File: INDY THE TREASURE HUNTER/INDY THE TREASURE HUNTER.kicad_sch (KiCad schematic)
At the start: 4 parts, among them J1 Conn_01x06, J2 Conn_01x06, J3 Conn_01x06, J4 Conn_01x06

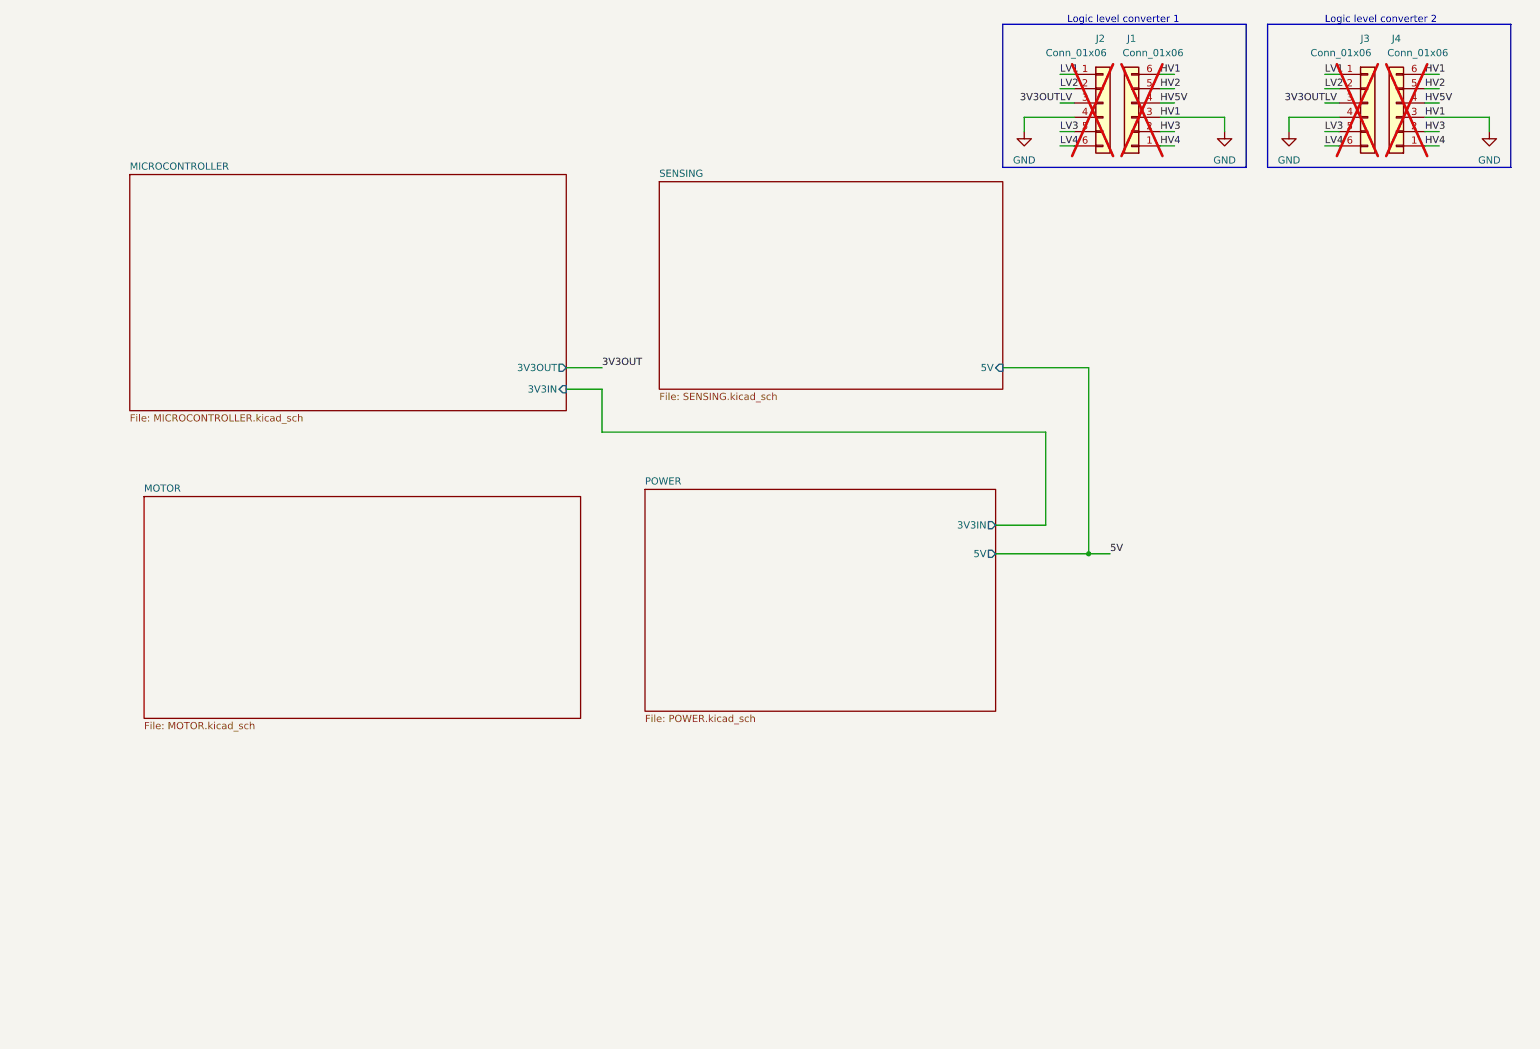
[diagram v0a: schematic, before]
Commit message: 19:16
Got rid of the boxes around the logic level converters, we can neaten those up later it was just becoming a nightmare.

Also IMPORTANT:
Try to stick with this naming convention for logic level lines: NAMEOFLINE_VOLTAGE (eg: ULTRA_TRIG_3V3) so we can track the logic level voltages
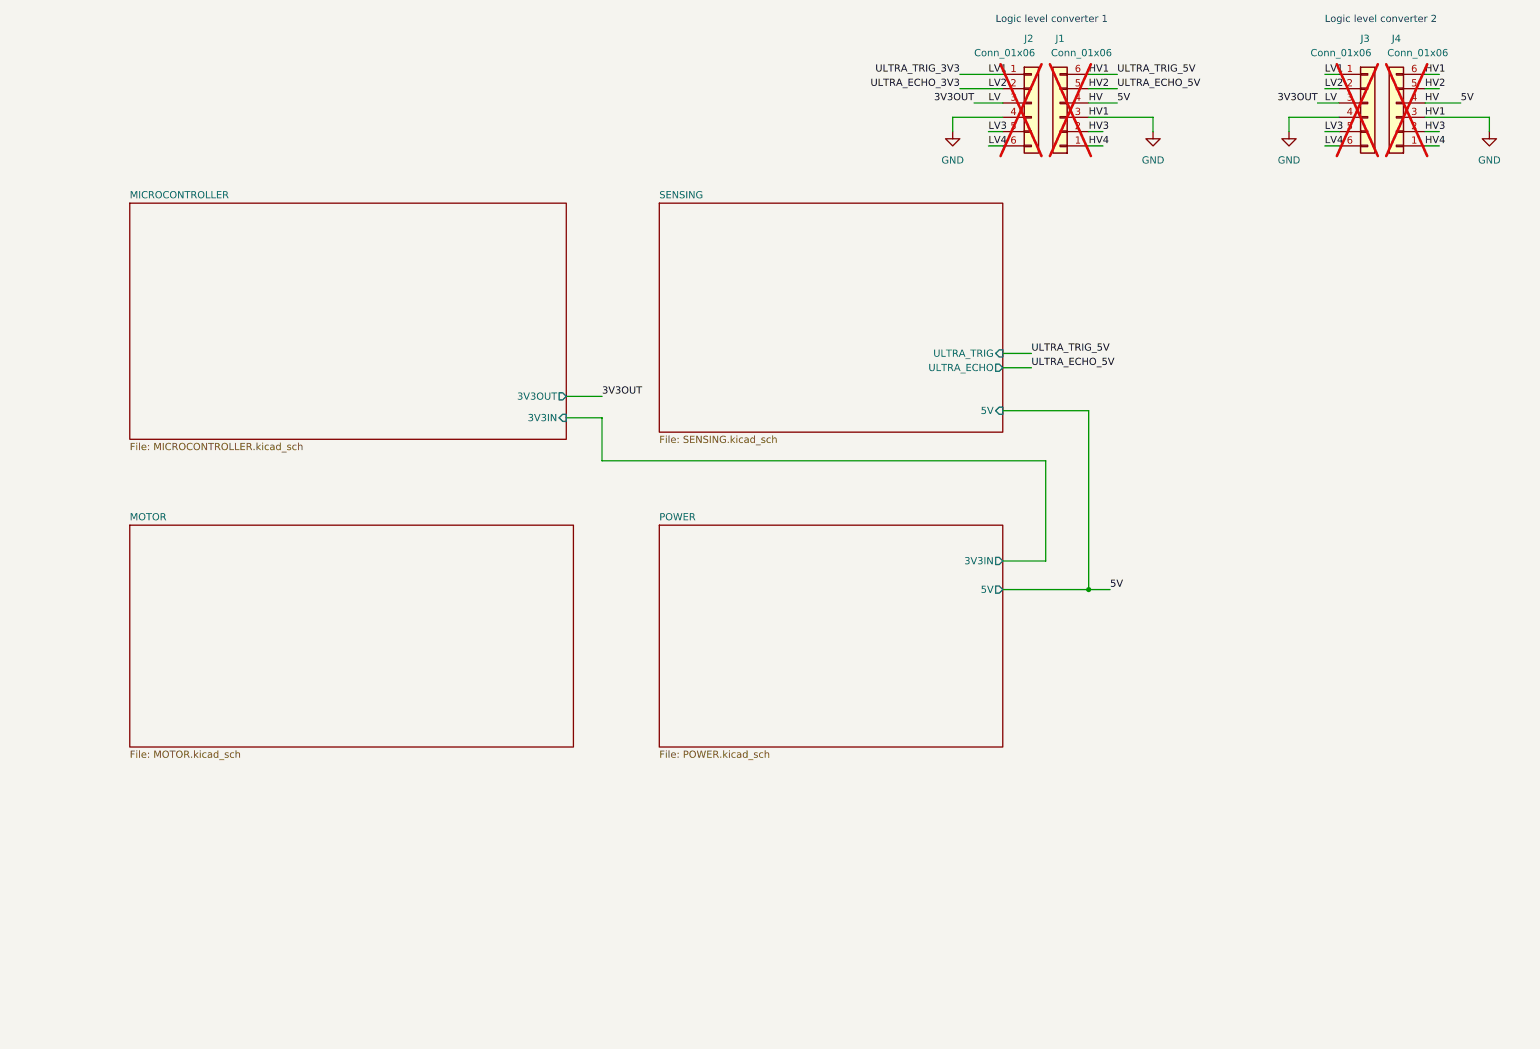
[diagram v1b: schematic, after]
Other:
- sheet SENSING ports: added ULTRA_ECHO, ULTRA_TRIG; removed none
- moved on the sheet: J1, J2

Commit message: Wired up Ultrasonic sensor
I think the USonic sensor is wired up completely. Not that bad actually.
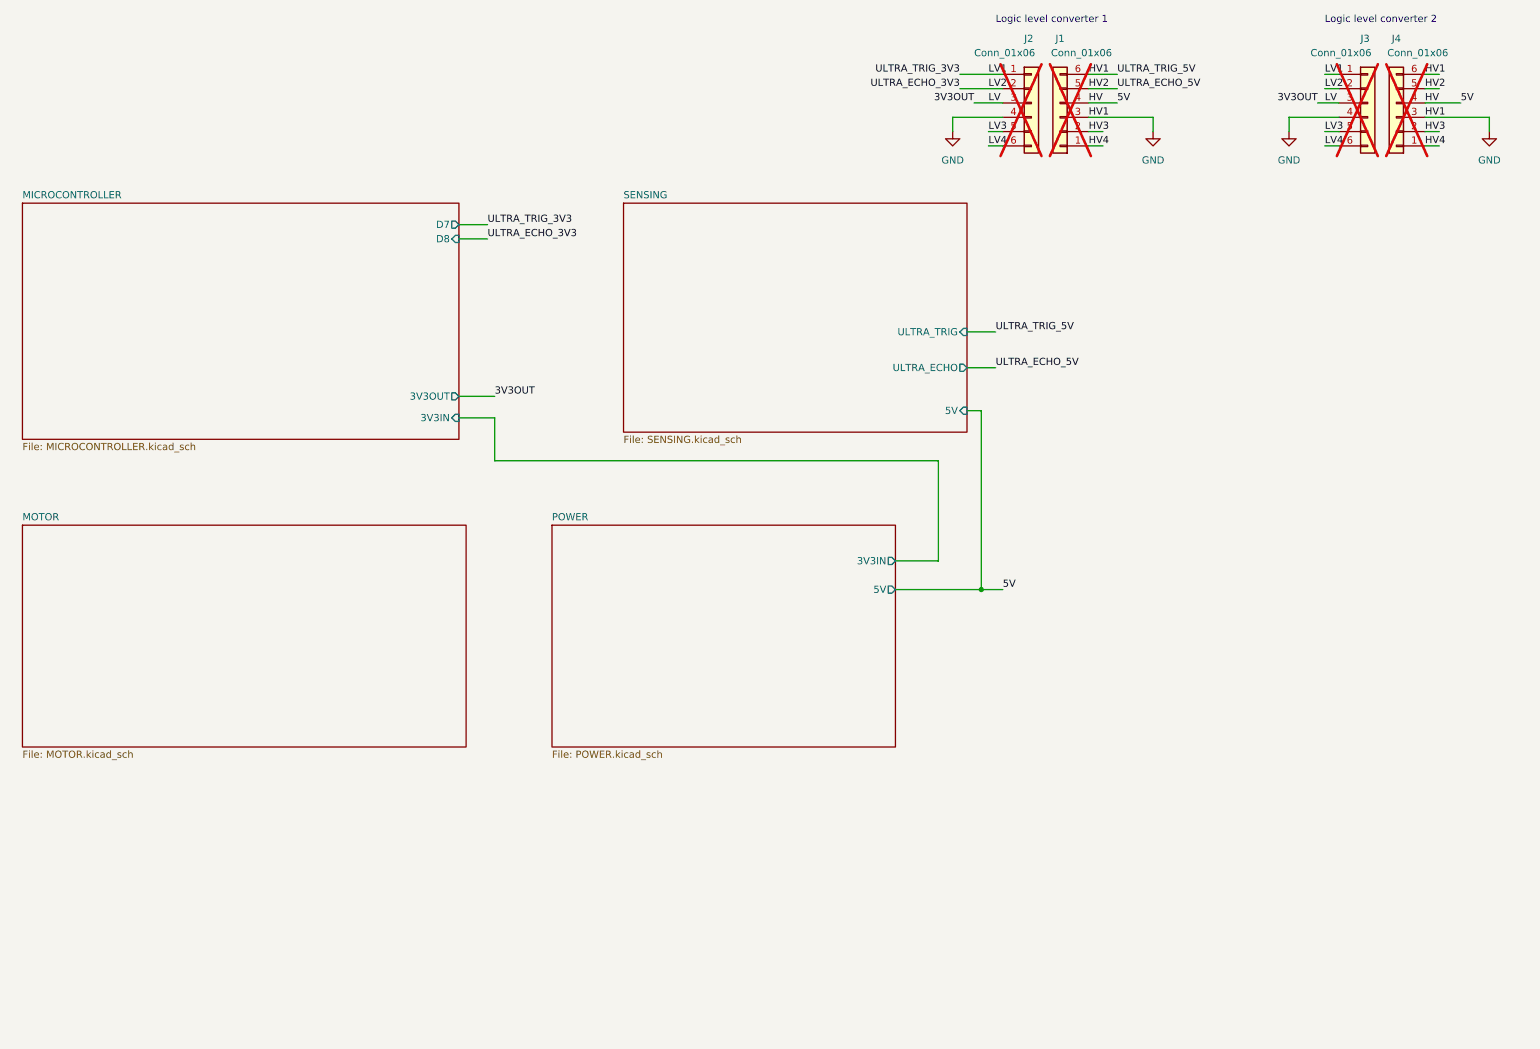
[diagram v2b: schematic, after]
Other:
- sheet MICROCONTROLLER ports: added D7, D8; removed none
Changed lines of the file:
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@@
 (kicad_sch (version 20230121) (generator eeschema)
   (paper "A4")
-  (junction (at 208.28 114.3) (diameter 0) (color 0 0 0 0)
+  (junction (at 189.23 114.3) (diameter 0) (color 0 0 0 0)
   )
   (wire (pts (xy 267.97 33.02) (xy 270.51 33.02))
@@
     (stroke (width 0) (type default))
   )
-  (wire (pts (xy 193.04 72.39) (xy 198.12 72.39))
-    (stroke (width 0) (type default))
-  )
-  (wire (pts (xy 115.57 80.01) (xy 121.92 80.01))
+  (wire (pts (xy 186.69 68.58) (xy 191.77 68.58))
+    (stroke (width 0) (type default))
+  )
+  (wire (pts (xy 96.52 80.01) (xy 102.87 80.01))
     (stroke (width 0) (type default))
   )
@@
     (stroke (width 0) (type default))
   )
-  (wire (pts (xy 121.92 91.44) (xy 200.66 91.44))
+  (wire (pts (xy 102.87 91.44) (xy 181.61 91.44))
     (stroke (width 0) (type default))
   )
@@
     (stroke (width 0) (type default))
   )
-  (wire (pts (xy 208.28 114.3) (xy 212.09 114.3))
+  (wire (pts (xy 189.23 114.3) (xy 193.04 114.3))
     (stroke (width 0) (type default))
   )
@@
     (stroke (width 0) (type default))
   )
-  (wire (pts (xy 193.04 114.3) (xy 208.28 114.3))
+  (wire (pts (xy 173.99 114.3) (xy 189.23 114.3))
     (stroke (width 0) (type default))
   )
@@
     (stroke (width 0) (type default))
   )
-  (wire (pts (xy 193.04 82.55) (xy 208.28 82.55))
+  (wire (pts (xy 96.52 52.07) (xy 101.6 52.07))
+    (stroke (width 0) (type default))
+  )
+  (wire (pts (xy 186.69 82.55) (xy 189.23 82.55))
     (stroke (width 0) (type default))
   )
@@
     (stroke (width 0) (type default))
   )
-  (wire (pts (xy 200.66 91.44) (xy 200.66 109.22))
-    (stroke (width 0) (type default))
-  )
-  (wire (pts (xy 121.92 91.44) (xy 121.92 83.82))
-    (stroke (width 0) (type default))
-  )
-  (wire (pts (xy 121.92 83.82) (xy 115.57 83.82))
-    (stroke (width 0) (type default))
-  )
-  (wire (pts (xy 193.04 109.22) (xy 200.66 109.22))
+  (wire (pts (xy 181.61 91.44) (xy 181.61 109.22))
+    (stroke (width 0) (type default))
+  )
+  (wire (pts (xy 102.87 91.44) (xy 102.87 83.82))
+    (stroke (width 0) (type default))
+  )
+  (wire (pts (xy 102.87 83.82) (xy 96.52 83.82))
+    (stroke (width 0) (type default))
+  )
+  (wire (pts (xy 173.99 109.22) (xy 181.61 109.22))
     (stroke (width 0) (type default))
   )
@@
     (stroke (width 0) (type default))
   )
-  (wire (pts (xy 208.28 82.55) (xy 208.28 114.3))
-    (stroke (width 0) (type default))
-  )
-  (wire (pts (xy 193.04 74.93) (xy 198.12 74.93))
+  (wire (pts (xy 189.23 82.55) (xy 189.23 114.3))
+    (stroke (width 0) (type default))
+  )
+  (wire (pts (xy 96.52 49.53) (xy 101.6 49.53))
+    (stroke (width 0) (type default))
+  )
+  (wire (pts (xy 186.69 74.93) (xy 191.77 74.93))
     (stroke (width 0) (type default))
   )
@@
     (effects (font (size 1.27 1.27)) (justify right bottom))
   )
+  (label "ULTRA_TRIG_3V3" (at 101.6 49.53 0) (fields_autoplaced)
+    (effects (font (size 1.27 1.27)) (justify left bottom))
+  )
   (label "HV1" (at 208.28 30.48 0) (fields_autoplaced)
     (effects (font (size 1.27 1.27)) (justify left bottom))
@@
     (effects (font (size 1.27 1.27)) (justify right bottom))
   )
-  (label "ULTRA_TRIG_5V" (at 198.12 72.39 0) (fields_autoplaced)
+  (label "ULTRA_TRIG_5V" (at 191.77 68.58 0) (fields_autoplaced)
     (effects (font (size 1.27 1.27)) (justify left bottom))
   )
@@
     (effects (font (size 1.27 1.27)) (justify left bottom))
   )
+  (label "ULTRA_ECHO_3V3" (at 101.6 52.07 0) (fields_autoplaced)
+    (effects (font (size 1.27 1.27)) (justify left bottom))
+  )
   (label "ULTRA_TRIG_5V" (at 213.36 22.86 0) (fields_autoplaced)
     (effects (font (size 1.27 1.27)) (justify left bottom))
@@
     (effects (font (size 1.27 1.27)) (justify left bottom))
   )
-  (label "5V" (at 212.09 114.3 0) (fields_autoplaced)
-    (effects (font (size 1.27 1.27)) (justify left bottom))
-  )
-  (label "ULTRA_ECHO_5V" (at 198.12 74.93 0) (fields_autoplaced)
+  (label "5V" (at 193.04 114.3 0) (fields_autoplaced)
+    (effects (font (size 1.27 1.27)) (justify left bottom))
+  )
+  (label "ULTRA_ECHO_5V" (at 191.77 74.93 0) (fields_autoplaced)
     (effects (font (size 1.27 1.27)) (justify left bottom))
   )
@@
     (effects (font (size 1.27 1.27)) (justify left bottom))
   )
-  (label "3V3OUT" (at 121.92 80.01 0) (fields_autoplaced)
+  (label "3V3OUT" (at 102.87 80.01 0) (fields_autoplaced)
     (effects (font (size 1.27 1.27)) (justify left bottom))
   )
@@
     )
   )
-  (sheet (at 38.1 102.87) (size 78.74 39.37) (fields_autoplaced)
+  (sheet (at 19.05 102.87) (size 78.74 39.37) (fields_autoplaced)
     (stroke (width 0.1524) (type solid))
     (fill (color 0 0 0 0.0000))
-    (property "Sheetname" "MOTOR" (at 38.1 102.1584 0)
+    (property "Sheetname" "MOTOR" (at 19.05 102.1584 0)
       (effects (font (size 1.27 1.27)) (justify left bottom))
     )
-    (property "Sheetfile" "MOTOR.kicad_sch" (at 38.1 142.8246 0)
+    (property "Sheetfile" "MOTOR.kicad_sch" (at 19.05 142.8246 0)
       (effects (font (size 1.27 1.27)) (justify left top))
     )
@@
     )
   )
-  (sheet (at 132.08 45.72) (size 60.96 40.64) (fields_autoplaced)
+  (sheet (at 125.73 45.72) (size 60.96 40.64) (fields_autoplaced)
     (stroke (width 0.1524) (type solid))
     (fill (color 0 0 0 0.0000))
-    (property "Sheetname" "SENSING" (at 132.08 45.0084 0)
+    (property "Sheetname" "SENSING" (at 125.73 45.0084 0)
       (effects (font (size 1.27 1.27)) (justify left bottom))
     )
-    (property "Sheetfile" "SENSING.kicad_sch" (at 132.08 86.9446 0)
+    (property "Sheetfile" "SENSING.kicad_sch" (at 125.73 86.9446 0)
       (effects (font (size 1.27 1.27)) (justify left top))
     )
-    (pin "5V" input (at 193.04 82.55 0)
-      (effects (font (size 1.27 1.27)) (justify right))
-    )
-    (pin "ULTRA_ECHO" output (at 193.04 74.93 0)
-      (effects (font (size 1.27 1.27)) (justify right))
-    )
-    (pin "ULTRA_TRIG" input (at 193.04 72.39 0)
+    (pin "5V" input (at 186.69 82.55 0)
+      (effects (font (size 1.27 1.27)) (justify right))
+    )
+    (pin "ULTRA_ECHO" output (at 186.69 74.93 0)
+      (effects (font (size 1.27 1.27)) (justify right))
+    )
+    (pin "ULTRA_TRIG" input (at 186.69 68.58 0)
       (effects (font (size 1.27 1.27)) (justify right))
     )
@@
     )
   )
-  (sheet (at 38.1 45.72) (size 77.47 41.91) (fields_autoplaced)
+  (sheet (at 19.05 45.72) (size 77.47 41.91) (fields_autoplaced)
     (stroke (width 0.1524) (type solid))
     (fill (color 0 0 0 0.0000))
-    (property "Sheetname" "MICROCONTROLLER" (at 38.1 45.0084 0)
+    (property "Sheetname" "MICROCONTROLLER" (at 19.05 45.0084 0)
       (effects (font (size 1.27 1.27)) (justify left bottom))
     )
-    (property "Sheetfile" "MICROCONTROLLER.kicad_sch" (at 38.1 88.2146 0)
+    (property "Sheetfile" "MICROCONTROLLER.kicad_sch" (at 19.05 88.2146 0)
       (effects (font (size 1.27 1.27)) (justify left top))
     )
-    (pin "3V3IN" input (at 115.57 83.82 0)
-      (effects (font (size 1.27 1.27)) (justify right))
-    )
-    (pin "3V3OUT" output (at 115.57 80.01 0)
+    (pin "3V3IN" input (at 96.52 83.82 0)
+      (effects (font (size 1.27 1.27)) (justify right))
+    )
+    (pin "3V3OUT" output (at 96.52 80.01 0)
+      (effects (font (size 1.27 1.27)) (justify right))
+    )
+    (pin "D8" input (at 96.52 52.07 0)
+      (effects (font (size 1.27 1.27)) (justify right))
+    )
+    (pin "D7" output (at 96.52 49.53 0)
       (effects (font (size 1.27 1.27)) (justify right))
     )
@@
     )
   )
-  (sheet (at 132.08 102.87) (size 60.96 39.37) (fields_autoplaced)
+  (sheet (at 113.03 102.87) (size 60.96 39.37) (fields_autoplaced)
     (stroke (width 0.1524) (type solid))
     (fill (color 0 0 0 0.0000))
-    (property "Sheetname" "POWER" (at 132.08 102.1584 0)
+    (property "Sheetname" "POWER" (at 113.03 102.1584 0)
       (effects (font (size 1.27 1.27)) (justify left bottom))
     )
-    (property "Sheetfile" "POWER.kicad_sch" (at 132.08 142.8246 0)
+    (property "Sheetfile" "POWER.kicad_sch" (at 113.03 142.8246 0)
       (effects (font (size 1.27 1.27)) (justify left top))
     )
-    (pin "5V" output (at 193.04 114.3 0)
-      (effects (font (size 1.27 1.27)) (justify right))
-    )
-    (pin "3V3IN" output (at 193.04 109.22 0)
-      (effects (font (size 1.27 1.27)) (justify right))
-    )
+    (pin "5V" output (at 173.99 114.3 0)
+      (effects (font (size 1.27 1.27)) (justify right))
+    )
+    (pin "3V3IN" output (at 173.99 109.22 0)
+      (effects (font (size 1.27 1.27)) (justify right))
+    )

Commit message: 00:53
Battery = done (?)
Motor control = done (no clue)
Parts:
- removed J1, J2, J3, J4: Conn_01x06, symbol Connector_Generic:Conn_01x06
- added J1, J2, J3, J6: Conn_01x06_Pin, symbol Connector:Conn_01x06_Pin
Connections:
- net 3V3OUT: now also J1.4 (Pin_4), J3.4 (Pin_4)
- net 5V: now also J2.3 (Pin_3), J6.3 (Pin_3)
- net GND: now also J1.3 (Pin_3), J2.1 (Pin_1), J2.4 (Pin_4), J3.3 (Pin_3), J6.1 (Pin_1), J6.4 (Pin_4)
- net HV2: now also J2.2 (Pin_2), J6.2 (Pin_2)
- net HV3: now also J2.5 (Pin_5), J6.5 (Pin_5)
- net HV4: now also J2.6 (Pin_6), J6.6 (Pin_6)
- net LV1: now also J1.6 (Pin_6), J3.6 (Pin_6)
- net LV2: now also J1.5 (Pin_5), J3.5 (Pin_5)
- net LV3: now also J1.2 (Pin_2), J3.2 (Pin_2)
- net LV4: now also J1.1 (Pin_1), J3.1 (Pin_1)
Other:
- sheet MOTOR ports: added 5V, MOT_CTRL_IN1, MOT_CTRL_IN2, MOT_CTRL_IN3, MOT_CTRL_IN4; removed none
- note added: "Logic level converter 2: motor control"
- note removed: "Logic level converter 2"
